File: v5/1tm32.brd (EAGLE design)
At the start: 50.8 x 50.8 mm, 44 parts, among them IC1 STM32L412RBT6P, J1 DST310S_32.768KHZ, J2 10118192-0001LF, U2 LD39050PU33R, Y1 8MHz

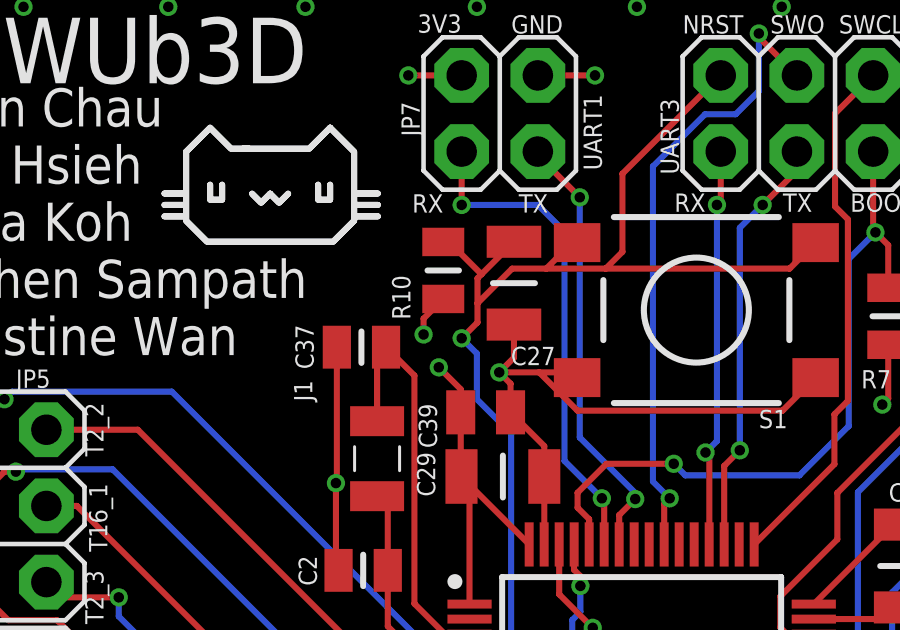
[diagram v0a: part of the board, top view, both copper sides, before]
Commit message: removed resistor for switch
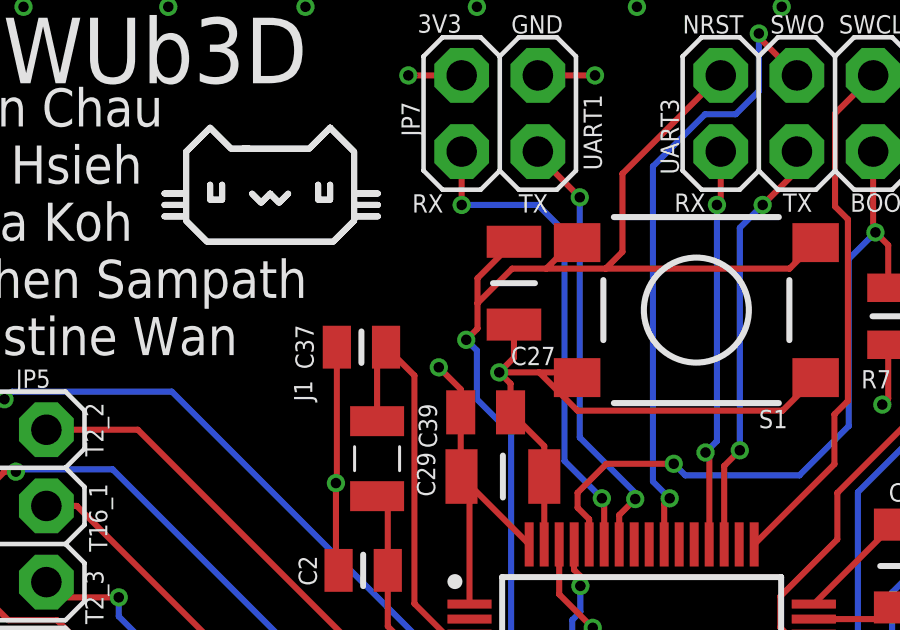
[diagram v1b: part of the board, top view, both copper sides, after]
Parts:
- removed R10: 10K, RC0805JR-0710KL:RESC2012X60N
- IC1: value STM32L412RBT6P -> STM32L412RBT6
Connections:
- net 3V3: no longer R10.2
- net NRST: no longer R10.1
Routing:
- net NRST: track 41.1 -> 39.3 mm
- net 3V3: track 63.7 -> 62.2 mm, vias 11 -> 10
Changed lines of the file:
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@@
 <attribute name="PRICE" value="None" x="31.228" y="52.511" size="1.778" layer="27" rot="R90" display="off"/>
 </element>
-<element name="IC1" library="STM32L412RBT6P" package="QFP50P1200X1200X160-64N" value="STM32L412RBT6P" x="26.193" y="25.744" smashed="yes">
+<element name="IC1" library="STM32L412RBT6P" package="QFP50P1200X1200X160-64N" value="STM32L412RBT6" x="26.193" y="25.744" smashed="yes">
 <attribute name="DESCRIPTION" value="ARM Microcontrollers - MCU" x="26.193" y="25.744" size="1.778" layer="27" display="off"/>
 <attribute name="HEIGHT" value="1.6mm" x="26.193" y="25.744" size="1.778" layer="27" display="off"/>
@@
 <attribute name="MOUSER_PRICE-STOCK" value="https://www.mouser.co.uk/ProductDetail/YAGEO/RC0805FR-131KL?qs=m6lXFsvg5e0qJLgmV7HC3Q%3D%3D" x="34.412" y="39.0882" size="1.778" layer="27" rot="R270" display="off"/>
 <attribute name="NAME" x="34.012" y="36.9882" size="0.6096" layer="25" align="center"/>
-</element>
-<element name="R10" library="RC0805JR-0710KL" package="RESC2012X60N" value="10K" x="19.5786" y="40.615" smashed="yes" rot="R270">
-<attribute name="DESCRIPTION" value="YAGEO - RC0805JR-0710KL - SMD Chip Resistor, 0805 [2012 Metric], 10 kohm, RC Series, 150 V, Thick Film, 125 mW" x="19.5786" y="40.615" size="1.778" layer="27" rot="R270" display="off"/>
-<attribute name="HEIGHT" value="0.6mm" x="19.5786" y="40.615" size="1.778" layer="27" rot="R270" display="off"/>
-<attribute name="MANUFACTURER_NAME" value="KEMET" x="19.5786" y="40.615" size="1.778" layer="27" rot="R270" display="off"/>
-<attribute name="MANUFACTURER_PART_NUMBER" value="RC0805JR-0710KL" x="19.5786" y="40.615" size="1.778" layer="27" rot="R270" display="off"/>
-<attribute name="MOUSER_PART_NUMBER" value="603-RC0805JR-0710KL" x="19.5786" y="40.615" size="1.778" layer="27" rot="R270" display="off"/>
-<attribute name="MOUSER_PRICE-STOCK" value="https://www.mouser.co.uk/ProductDetail/YAGEO/RC0805JR-0710KL?qs=ZFGQJeMQzF5q%2Fp77vM%2FrVQ%3D%3D" x="19.5786" y="40.615" size="1.778" layer="27" rot="R270" display="off"/>
-<attribute name="NAME" x="18.1786" y="39.715" size="0.6096" layer="25" rot="R90" align="center"/>
 </element>
 <element name="R1" library="RC0805FR-131KL" package="RESC2012X60N" value="1K" x="38.977" y="43.338" smashed="yes" rot="R90">
@@
 </polygon>
 <contactref element="R6" pad="2"/>
-<contactref element="R10" pad="2"/>
 <wire x1="34.798" y1="5.2" x2="34.798" y2="5.327" width="0.2032" layer="1"/>
 <wire x1="23.443" y1="20.006" x2="23.443" y2="16.019" width="0.2032" layer="1"/>
@@
 <wire x1="20.193" y1="47.117" x2="18.415" y2="47.117" width="0.2032" layer="1"/>
 <via x="18.415" y="47.117" extent="1-16" drill="0.35"/>
-<wire x1="19.5786" y1="39.665" x2="18.923" y2="39.0094" width="0.2032" layer="1"/>
-<wire x1="18.923" y1="39.0094" x2="18.923" y2="38.481" width="0.2032" layer="1"/>
-<via x="18.923" y="38.481" extent="1-16" drill="0.35"/>
 <wire x1="37.253" y1="32.117" x2="38.721" y2="32.117" width="0.2032" layer="1"/>
 <wire x1="38.721" y1="32.117" x2="38.862" y2="32.258" width="0.2032" layer="1"/>
@@
 <contactref element="IC1" pad="7"/>
 <contactref element="C27" pad="2"/>
-<contactref element="R10" pad="1"/>
 <contactref element="JP3" pad="2"/>
 <via x="21.844" y="26.4888" extent="1-16" drill="0.35"/>
@@
 <wire x1="21.844" y1="26.4888" x2="20.4602" y2="26.4888" width="0.2032" layer="1"/>
 <wire x1="21.844" y1="35.179" x2="20.701" y2="36.322" width="0.2032" layer="16"/>
-<wire x1="20.193" y1="38.354" x2="20.701" y2="37.846" width="0.2032" layer="16"/>
-<wire x1="20.701" y1="37.846" x2="20.701" y2="36.322" width="0.2032" layer="16"/>
+<wire x1="20.3454" y1="38.3032" x2="20.701" y2="37.9476" width="0.2032" layer="16"/>
+<wire x1="20.701" y1="37.9476" x2="20.701" y2="36.322" width="0.2032" layer="16"/>
 <wire x1="21.844" y1="35.179" x2="21.844" y2="26.4888" width="0.2032" layer="16"/>
-<wire x1="19.812" y1="41.565" x2="19.5786" y2="41.565" width="0.2032" layer="1"/>
-<via x="20.193" y="38.354" extent="1-16" drill="0.35"/>
-<wire x1="20.193" y1="38.354" x2="20.7212" y2="38.8822" width="0.2032" layer="1"/>
-<wire x1="20.7212" y1="40.3562" x2="20.853" y2="40.488" width="0.2032" layer="1"/>
-<wire x1="20.853" y1="40.488" x2="21.936" y2="41.571" width="0.2032" layer="1"/>
-<wire x1="20.7212" y1="38.8822" x2="20.7212" y2="39.5224" width="0.2032" layer="1"/>
+<via x="20.3454" y="38.3032" extent="1-16" drill="0.35"/>
+<wire x1="20.3454" y1="38.3032" x2="20.7212" y2="38.679" width="0.2032" layer="1"/>
+<wire x1="20.7212" y1="40.3562" x2="21.936" y2="41.571" width="0.2032" layer="1"/>
+<wire x1="20.7212" y1="38.679" x2="20.7212" y2="39.5224" width="0.2032" layer="1"/>
 <wire x1="20.7212" y1="39.5224" x2="20.7212" y2="40.3562" width="0.2032" layer="1"/>
-<wire x1="20.853" y1="40.488" x2="19.812" y2="41.529" width="0.2032" layer="1"/>
-<wire x1="19.812" y1="41.529" x2="19.812" y2="41.565" width="0.2032" layer="1"/>
 <wire x1="20.7212" y1="39.5224" x2="21.875" y2="40.6762" width="0.2032" layer="1"/>
 <contactref element="S1" pad="2"/>
